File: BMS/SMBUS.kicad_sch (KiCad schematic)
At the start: 4 parts

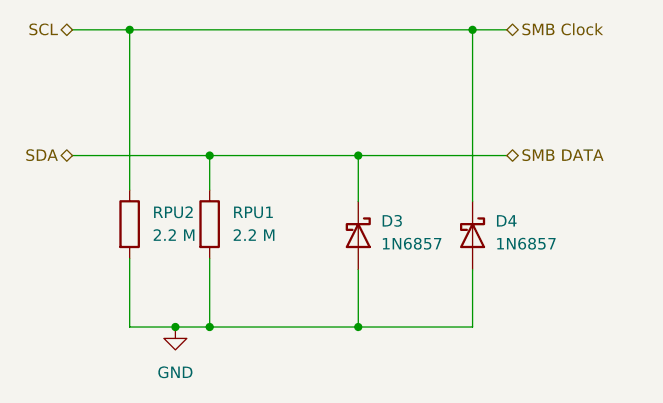
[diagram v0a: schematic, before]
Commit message: DCDC fix unavailable parts, BMS redesign, handle fix, rearrange top half
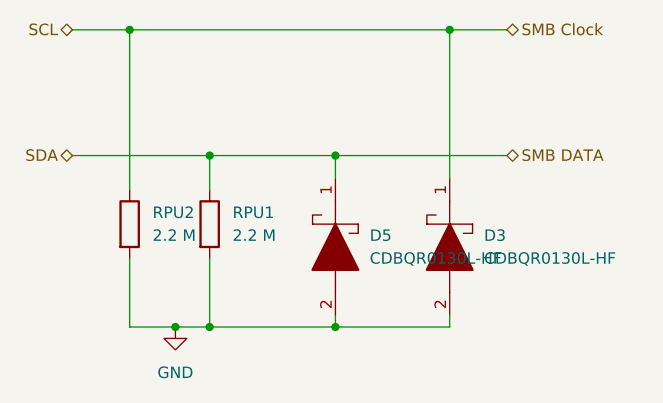
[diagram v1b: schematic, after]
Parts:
- removed D3, D4: 1N6857, Diode_THT:D_DO-35_SOD27_P7.62mm_Horizontal, symbol Diode:1N6857
- added D3, D5: CDBQR0130L-HF, Diode_SMD:D_0402_1005Metric, symbol Local:CDBWL521-HF
- RPU1, RPU2: footprint (none) -> Resistor_SMD:R_2010_5025Metric; Manufacturer_Part_Number (none) -> RCV20102M20JNEF
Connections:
- net GND: now also D3.2, D5.2
- net SCL: now also D3.1
- net SDA: now also D5.1
